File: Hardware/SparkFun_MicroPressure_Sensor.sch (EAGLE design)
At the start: 25 parts, among them J1 Qwiic, J2 Qwiic, U1 MPR_Pressure_Sensor

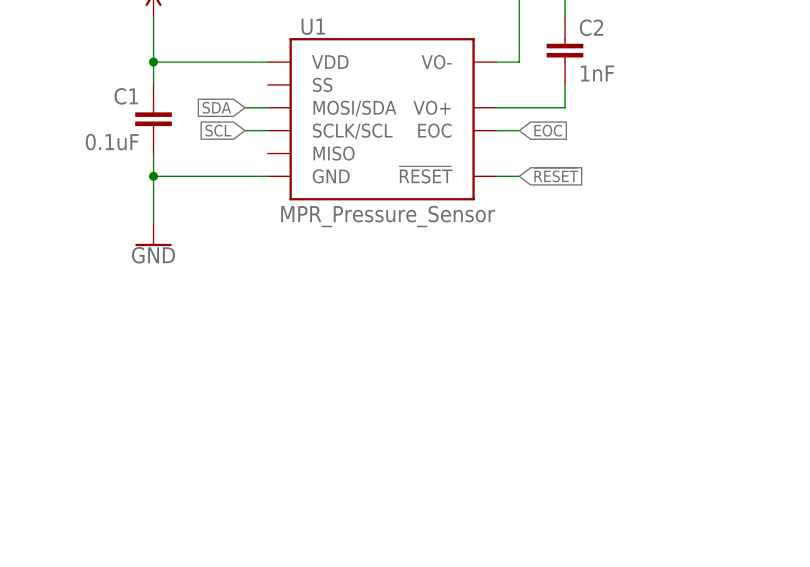
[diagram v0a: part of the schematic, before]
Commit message: v01 Update
- Added address to schematic, and pcb files
- Rerouted 3.3V trace for better ground pour.
- Updated MPR footprint silk
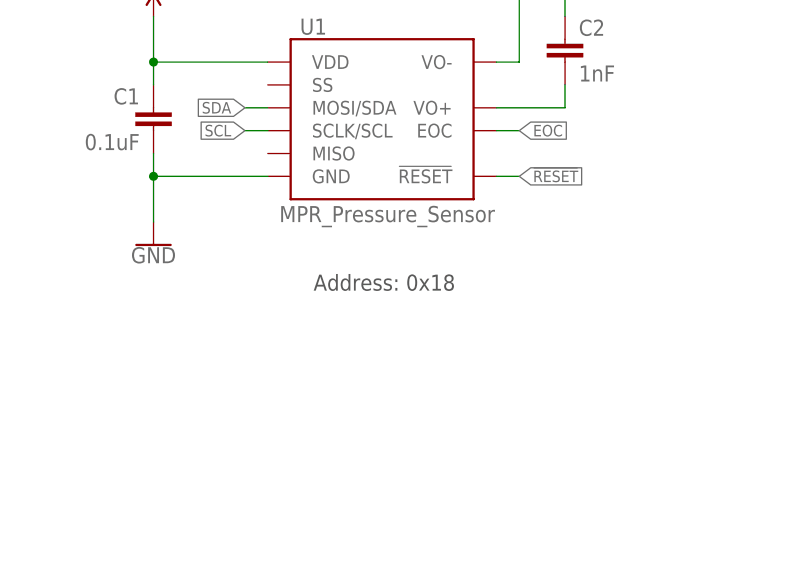
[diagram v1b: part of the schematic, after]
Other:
- note added: "Address: 0x18"
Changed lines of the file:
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@@
 <grid distance="0.1" unitdist="inch" unit="inch" style="lines" multiple="1" display="no" altdistance="0.01" altunitdist="inch" altunit="inch"/>
 <layers>
-<layer number="1" name="Top" color="4" fill="1" visible="yes" active="no"/>
-<layer number="2" name="Route2" color="16" fill="1" visible="yes" active="no"/>
-<layer number="15" name="Route15" color="23" fill="1" visible="yes" active="no"/>
-<layer number="16" name="Bottom" color="1" fill="1" visible="yes" active="no"/>
-<layer number="17" name="Pads" color="2" fill="1" visible="yes" active="no"/>
-<layer number="18" name="Vias" color="2" fill="1" visible="yes" active="no"/>
-<layer number="19" name="Unrouted" color="6" fill="1" visible="yes" active="no"/>
-<layer number="20" name="Dimension" color="24" fill="1" visible="yes" active="no"/>
-<layer number="21" name="tPlace" color="16" fill="1" visible="yes" active="no"/>
-<layer number="22" name="bPlace" color="14" fill="1" visible="yes" active="no"/>
-<layer number="23" name="tOrigins" color="15" fill="1" visible="yes" active="no"/>
-<layer number="24" name="bOrigins" color="15" fill="1" visible="yes" active="no"/>
-<layer number="25" name="tNames" color="7" fill="1" visible="yes" active="no"/>
-<layer number="26" name="bNames" color="7" fill="1" visible="yes" active="no"/>
-<layer number="27" name="tValues" color="7" fill="1" visible="yes" active="no"/>
-<layer number="28" name="bValues" color="7" fill="1" visible="yes" active="no"/>
+<layer number="1" name="Top" color="4" fill="1" visible="no" active="no"/>
+<layer number="2" name="Route2" color="16" fill="1" visible="no" active="no"/>
+<layer number="15" name="Route15" color="23" fill="1" visible="no" active="no"/>
+<layer number="16" name="Bottom" color="1" fill="1" visible="no" active="no"/>
+<layer number="17" name="Pads" color="2" fill="1" visible="no" active="no"/>
+<layer number="18" name="Vias" color="2" fill="1" visible="no" active="no"/>
+<layer number="19" name="Unrouted" color="6" fill="1" visible="no" active="no"/>
+<layer number="20" name="Dimension" color="24" fill="1" visible="no" active="no"/>
+<layer number="21" name="tPlace" color="16" fill="1" visible="no" active="no"/>
+<layer number="22" name="bPlace" color="14" fill="1" visible="no" active="no"/>
+<layer number="23" name="tOrigins" color="15" fill="1" visible="no" active="no"/>
+<layer number="24" name="bOrigins" color="15" fill="1" visible="no" active="no"/>
+<layer number="25" name="tNames" color="7" fill="1" visible="no" active="no"/>
+<layer number="26" name="bNames" color="7" fill="1" visible="no" active="no"/>
+<layer number="27" name="tValues" color="7" fill="1" visible="no" active="no"/>
+<layer number="28" name="bValues" color="7" fill="1" visible="no" active="no"/>
 <layer number="29" name="tStop" color="7" fill="3" visible="no" active="no"/>
 <layer number="30" name="bStop" color="7" fill="6" visible="no" active="no"/>
@@
 <layer number="35" name="tGlue" color="7" fill="4" visible="no" active="no"/>
 <layer number="36" name="bGlue" color="7" fill="5" visible="no" active="no"/>
-<layer number="37" name="tTest" color="7" fill="1" visible="yes" active="no"/>
-<layer number="38" name="bTest" color="7" fill="1" visible="yes" active="no"/>
+<layer number="37" name="tTest" color="7" fill="1" visible="no" active="no"/>
+<layer number="38" name="bTest" color="7" fill="1" visible="no" active="no"/>
 <layer number="39" name="tKeepout" color="4" fill="11" visible="no" active="no"/>
 <layer number="40" name="bKeepout" color="1" fill="11" visible="no" active="no"/>
@@
 <layer number="44" name="Drills" color="7" fill="1" visible="no" active="no"/>
 <layer number="45" name="Holes" color="7" fill="1" visible="no" active="no"/>
-<layer number="46" name="Milling" color="3" fill="1" visible="yes" active="no"/>
-<layer number="47" name="Measures" color="7" fill="1" visible="yes" active="no"/>
-<layer number="48" name="Document" color="7" fill="1" visible="yes" active="no"/>
-<layer number="49" name="Reference" color="7" fill="1" visible="yes" active="no"/>
-<layer number="50" name="dxf" color="7" fill="1" visible="yes" active="no"/>
-<layer number="51" name="tDocu" color="6" fill="1" visible="yes" active="no"/>
-<layer number="52" name="bDocu" color="7" fill="1" visible="yes" active="no"/>
-<layer number="53" name="tGND_GNDA" color="7" fill="9" visible="yes" active="no"/>
-<layer number="54" name="bGND_GNDA" color="1" fill="9" visible="yes" active="no"/>
-<layer number="56" name="wert" color="7" fill="1" visible="yes" active="no"/>
-<layer number="57" name="tCAD" color="7" fill="1" visible="yes" active="no"/>
-<layer number="59" name="tCarbon" color="7" fill="1" visible="yes" active="no"/>
-<layer number="60" name="bCarbon" color="7" fill="1" visible="yes" active="no"/>
+<layer number="46" name="Milling" color="3" fill="1" visible="no" active="no"/>
+<layer number="47" name="Measures" color="7" fill="1" visible="no" active="no"/>
+<layer number="48" name="Document" color="7" fill="1" visible="no" active="no"/>
+<layer number="49" name="Reference" color="7" fill="1" visible="no" active="no"/>
+<layer number="50" name="dxf" color="7" fill="1" visible="no" active="no"/>
+<layer number="51" name="tDocu" color="6" fill="1" visible="no" active="no"/>
+<layer number="52" name="bDocu" color="7" fill="1" visible="no" active="no"/>
+<layer number="53" name="tGND_GNDA" color="7" fill="9" visible="no" active="no"/>
+<layer number="54" name="bGND_GNDA" color="1" fill="9" visible="no" active="no"/>
+<layer number="56" name="wert" color="7" fill="1" visible="no" active="no"/>
+<layer number="57" name="tCAD" color="7" fill="1" visible="no" active="no"/>
+<layer number="59" name="tCarbon" color="7" fill="1" visible="no" active="no"/>
+<layer number="60" name="bCarbon" color="7" fill="1" visible="no" active="no"/>
 <layer number="88" name="SimResults" color="9" fill="1" visible="yes" active="yes"/>
 <layer number="89" name="SimProbes" color="9" fill="1" visible="yes" active="yes"/>
@@
 <text x="238.76" y="7.62" size="2.54" layer="94" font="vector">V01</text>
 <text x="165.354" y="11.176" size="2.54" layer="94" font="vector">Alex Wende</text>
+<text x="58.42" y="116.84" size="1.778" layer="97">Address: 0x18</text>
 </plain>
 <instances>

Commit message: V10
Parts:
- added R4: 2.2k, SparkFun-Resistors:2.2KOHM-0603-1/10W-1%
- FD1, FD2, FD3, FD4: value FIDUCIAL1X2 -> FIDUCIALUFIDUCIAL; device SparkFun-Aesthetics:FIDUCIAL1X2 -> SparkFun-Aesthetics:FIDUCIALUFIDUCIAL
- R1, R2: value 4.7k -> 2.2k; device SparkFun-Resistors:4.7KOHM-0603-1/10W-1% -> SparkFun-Resistors:2.2KOHM-0603-1/10W-1%
- U1: value MPR_Pressure_Sensor -> MPR Series; device MPR_Temp:MPR_PRESSURE_SENSOR -> SparkFun-Sensors:MPR_SERIES_PRESSURE_I2C
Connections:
- new net MISO: U1.MISO
- new net SS: U1.SS
- net !RESET: now also R4.2
- net 3.3V: now also R4.1
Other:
- note added: "Supply Voltage: 1.8 - 3.6V"
- note added: "V10"
- note removed: "V01"
- moved on the sheet: C1, C2, U1
